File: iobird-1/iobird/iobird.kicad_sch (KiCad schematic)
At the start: 20 parts, among them J1 USB-C, J2 Conn_01x40, U1 RP2040, U2 W25Q32JVSS, Y1 Xtal

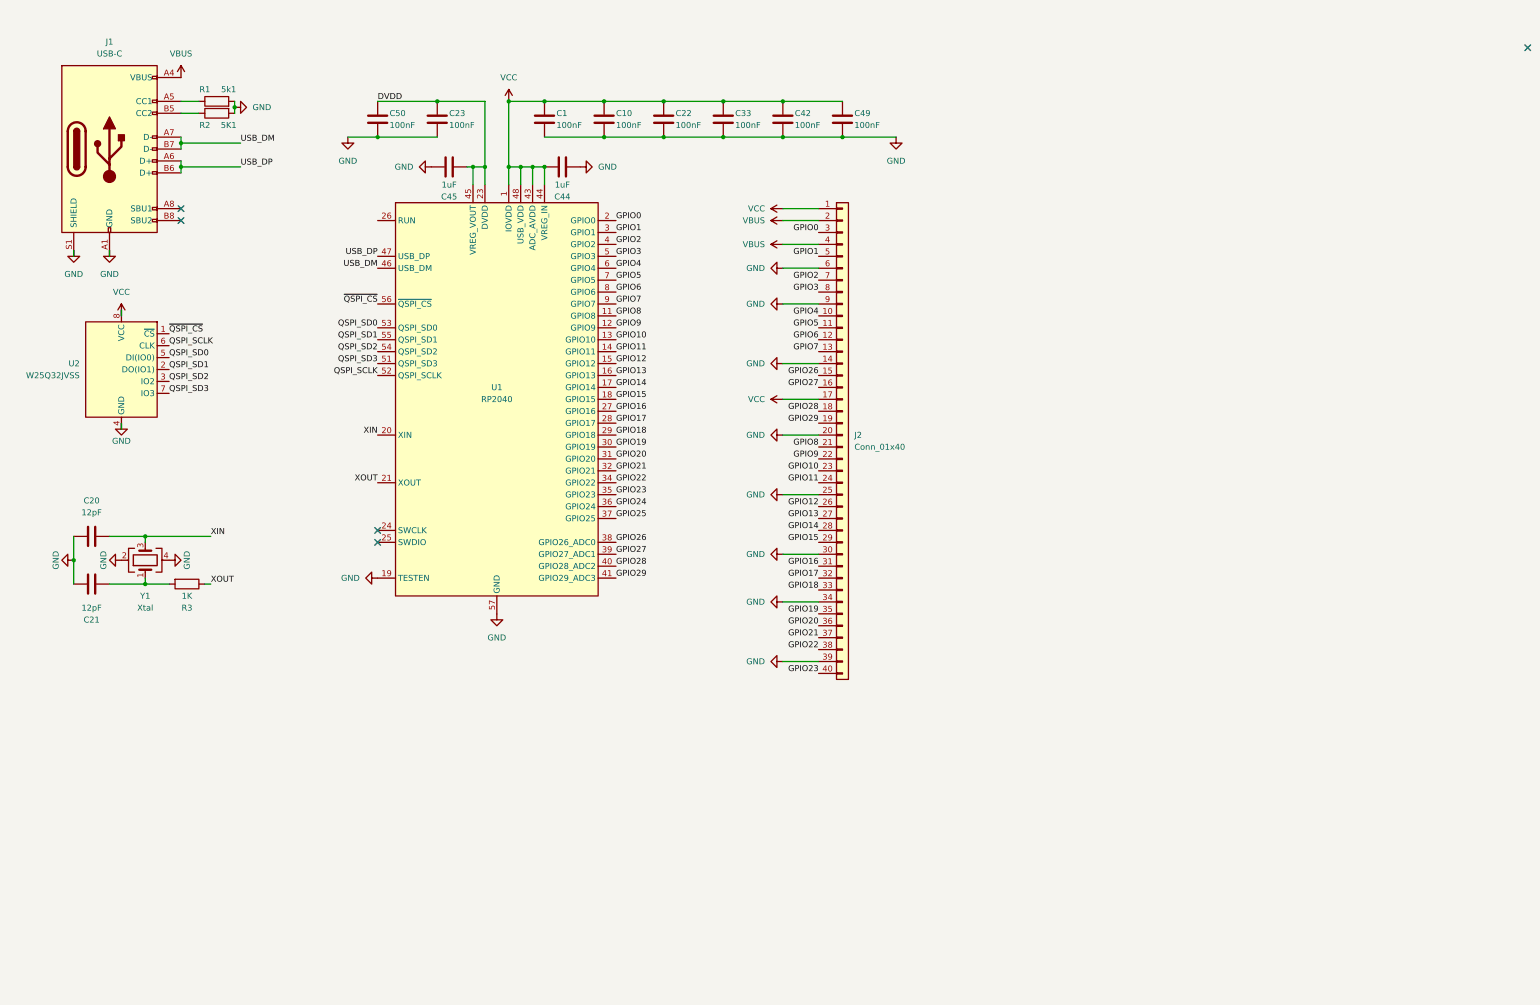
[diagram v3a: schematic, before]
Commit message: schematic layout improvements
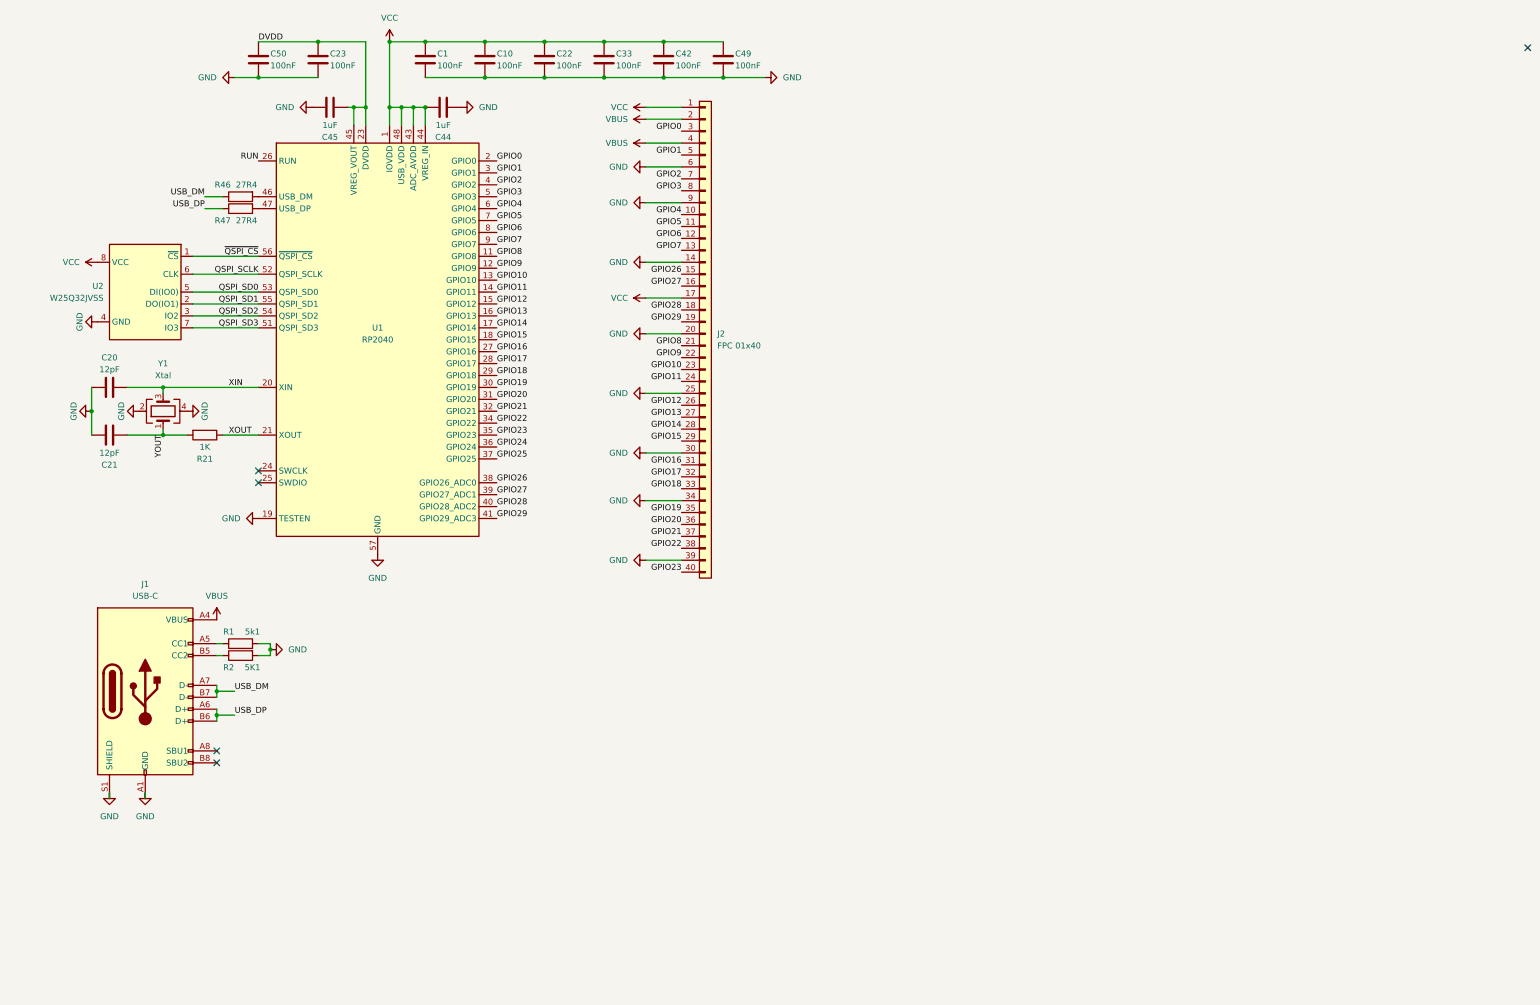
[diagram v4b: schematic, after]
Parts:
- added R46, R47: 27R4, symbol Device:R
- J2: value Conn_01x40 -> FPC 01x40
- renumbered R3 to R21
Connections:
- net USB_DM: now also R46.1; no longer U1.46 (USB_DM)
- net USB_DP: now also R47.1; no longer U1.47 (USB_DP)
- net YOUT: now reaches C21.2, R21.2, Y1.1
- net RUN: now reaches U1.26 (RUN)
- new net: R46.2, U1.46 (USB_DM)
- new net: R47.2, U1.47 (USB_DP)
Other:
- moved on the sheet: C1, C10, C20, C21, C22, C23, C33, C42, C44, C45, C49, C50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

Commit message: buttons and things
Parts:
- added C8: 100nF, symbol Device:C
- added D1: NSR0530HT1G, symbol Device:D_Schottky
- added R26, R3, R36, R56: 10k, symbol Device:R
- added R4: 1k, symbol Device:R
- added SW26: RESET, symbol Switch:SW_Push
- added SW56: BOOT, symbol Switch:SW_Push
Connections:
- net GND: now also C8.1, SW26.2, SW56.2
- net GPIO24: now also R36.2
- net RUN: now also R26.2, SW26.1
- net VCC: now also C8.2, R26.1, R3.1, R56.1
- net ~{QSPI_CS}: now also D1.2 (A), R56.2
- new net: D1.1 (K), R4.1
- new net: R3.2, R36.1, R4.2, SW56.1
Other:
- note added: "brain"
- note added: "decoupling capacitors"
- note added: "diverse devices"
- note added: "flash aah-aah"
- note added: "outside world"
- note added: "run stop"
- note added: "tick tock clock"
- note added: "user button"

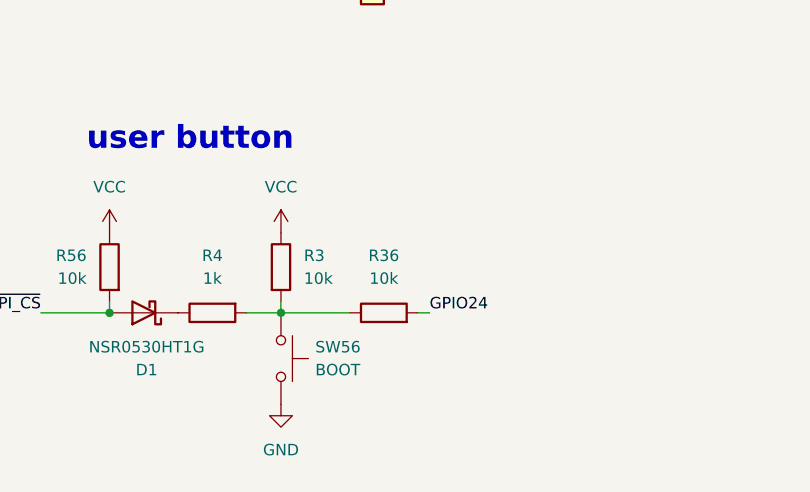
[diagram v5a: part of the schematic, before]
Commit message: adafruit-style bootsel instead of pimoroni-style
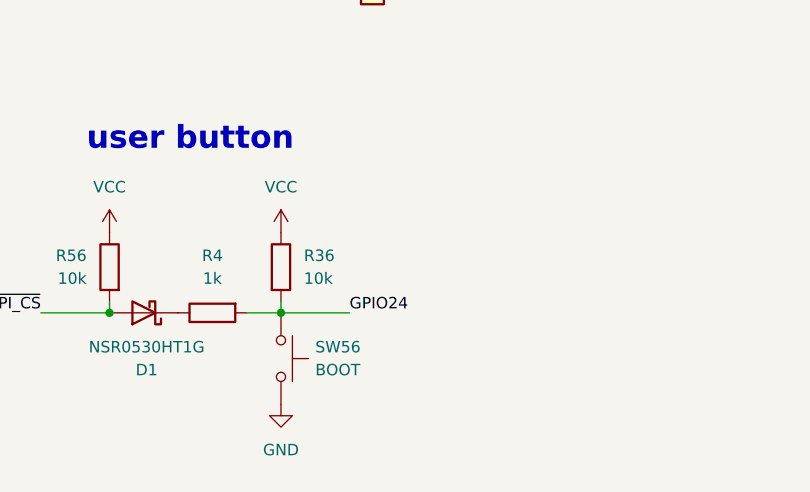
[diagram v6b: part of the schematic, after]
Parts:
- removed R36: 10k, symbol Device:R
- renumbered R3 to R36
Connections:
- net GPIO24: now also R36.2, R4.2, SW56.1
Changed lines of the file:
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@@
-    (stroke (width 0) (type default))
-  )
-  (wire (pts (xy 173.99 170.18) (xy 172.72 170.18))
     (stroke (width 0) (type default))
   )
@@
     (effects (font (size 1.27 1.27)) (justify left bottom))
   )
-  (label "GPIO24" (at 173.99 170.18 0) (fields_autoplaced)
+  (label "GPIO24" (at 165.1 170.18 0) (fields_autoplaced)
     (effects (font (size 1.27 1.27)) (justify left bottom))
   )
@@
         (path "/227befc9-6310-476c-924a-cf7b196aa881"
           (reference "SW26") (unit 1)
-        )
-      )
-    )
-  )
-  (symbol (lib_id "Device:R") (at 168.91 170.18 90) (unit 1)
-    (in_bom yes) (on_board yes) (dnp no) (fields_autoplaced)
-    (property "Reference" "R36" (at 168.91 163.83 90)
-      (effects (font (size 1.27 1.27)))
-    )
-    (property "Value" "10k" (at 168.91 166.37 90)
-      (effects (font (size 1.27 1.27)))
-    )
-    (property "Footprint" "" (at 168.91 171.958 90)
-      (effects (font (size 1.27 1.27)) hide)
-    )
-    (property "Datasheet" "~" (at 168.91 170.18 0)
-      (effects (font (size 1.27 1.27)) hide)
-    )
-    (pin "2")
-    (pin "1")
-    (instances
-      (project "iobird"
-        (path "/227befc9-6310-476c-924a-cf7b196aa881"
-          (reference "R36") (unit 1)
         )
       )
@@
   (symbol (lib_id "Device:R") (at 157.48 165.1 0) (unit 1)
     (in_bom yes) (on_board yes) (dnp no) (fields_autoplaced)
-    (property "Reference" "R3" (at 160.02 163.83 0)
+    (property "Reference" "R36" (at 160.02 163.83 0)
       (effects (font (size 1.27 1.27)) (justify left))
     )
@@
       (project "iobird"
         (path "/227befc9-6310-476c-924a-cf7b196aa881"
-          (reference "R3") (unit 1)
-        )
-      )
+          (reference "R36") (unit 1)
+        )
+      )

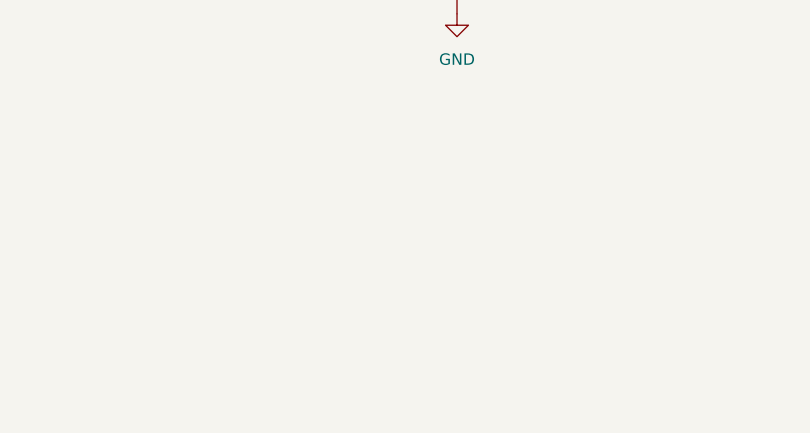
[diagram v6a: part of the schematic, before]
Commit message: add a neopixel
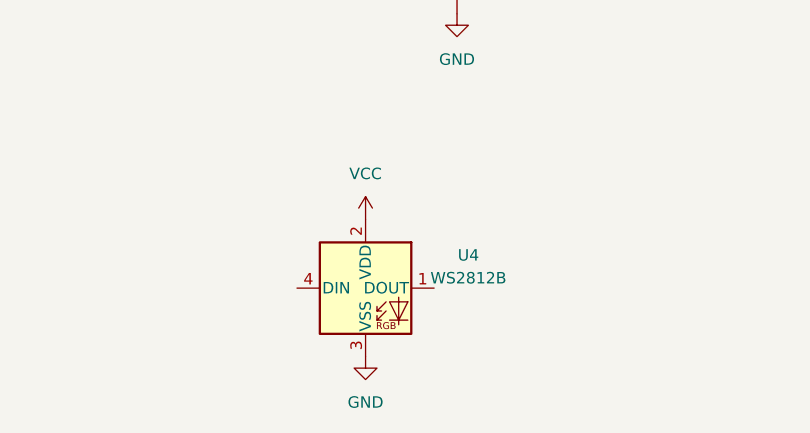
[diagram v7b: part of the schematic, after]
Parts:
- added U4: WS2812B, LED_SMD:LED_WS2812B_PLCC4_5.0x5.0mm_P3.2mm, symbol LED:WS2812B
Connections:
- net GND: now also U4.3 (VSS)
- net VCC: now also U4.2 (VDD)
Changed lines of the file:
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@@
+    )
+  )
+  (symbol (lib_id "power:GND") (at 147.32 218.44 0) (unit 1)
+    (in_bom yes) (on_board yes) (dnp no) (fields_autoplaced)
+    (property "Reference" "#PWR035" (at 147.32 224.79 0)
+      (effects (font (size 1.27 1.27)) hide)
+    )
+    (property "Value" "GND" (at 147.32 223.52 0)
+      (effects (font (size 1.27 1.27)))
+    )
+    (property "Footprint" "" (at 147.32 218.44 0)
+      (effects (font (size 1.27 1.27)) hide)
+    )
+    (property "Datasheet" "" (at 147.32 218.44 0)
+      (effects (font (size 1.27 1.27)) hide)
+    )
+    (pin "1")
+    (instances
+      (project "iobird"
+        (path "/227befc9-6310-476c-924a-cf7b196aa881"
+          (reference "#PWR035") (unit 1)
+        )
+      )
     )
   )
@@
         (path "/227befc9-6310-476c-924a-cf7b196aa881"
           (reference "R56") (unit 1)
+        )
+      )
+    )
+  )
+  (symbol (lib_id "LED:WS2812B") (at 147.32 210.82 0) (unit 1)
+    (in_bom yes) (on_board yes) (dnp no) (fields_autoplaced)
+    (property "Reference" "U4" (at 158.75 207.1721 0)
+      (effects (font (size 1.27 1.27)))
+    )
+    (property "Value" "WS2812B" (at 158.75 209.7121 0)
+      (effects (font (size 1.27 1.27)))
+    )
+    (property "Footprint" "LED_SMD:LED_WS2812B_PLCC4_5.0x5.0mm_P3.2mm" (at 148.59 218.44 0)
+      (effects (font (size 1.27 1.27)) (justify left top) hide)
+    )
+    (property "Datasheet" "https://cdn-shop.adafruit.com/datasheets/WS2812B.pdf" (at 149.86 220.345 0)
+      (effects (font (size 1.27 1.27)) (justify left top) hide)
+    )
+    (pin "1")
+    (pin "2")
+    (pin "3")
+    (pin "4")
+    (instances
+      (project "iobird"
+        (path "/227befc9-6310-476c-924a-cf7b196aa881"
+          (reference "U4") (unit 1)
         )
       )
@@
         )
       )
+    )
+  )
+  (symbol (lib_id "power:VCC") (at 147.32 203.2 0) (unit 1)
+    (in_bom yes) (on_board yes) (dnp no) (fields_autoplaced)
+    (property "Reference" "#PWR036" (at 147.32 207.01 0)
+      (effects (font (size 1.27 1.27)) hide)
+    )
+    (property "Value" "VCC" (at 147.32 198.12 0)
+      (effects (font (size 1.27 1.27)))
+    )
+    (property "Footprint" "" (at 147.32 203.2 0)
+      (effects (font (size 1.27 1.27)) hide)
+    )
+    (property "Datasheet" "" (at 147.32 203.2 0)
+      (effects (font (size 1.27 1.27)) hide)
+    )
+    (pin "1")
+    (instances
+      (project "iobird"
+        (path "/227befc9-6310-476c-924a-cf7b196aa881"
+          (reference "#PWR036") (unit 1)
+        )
+      )
